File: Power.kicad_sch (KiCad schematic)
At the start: 70 parts, among them J11 Conn_01x02_Socket, Q3 2N2222, U19 TPS25983, U20 SiA462DJ, U21 MIC23201YML-TR, U29 AP7361C-33E, U30 MP8795

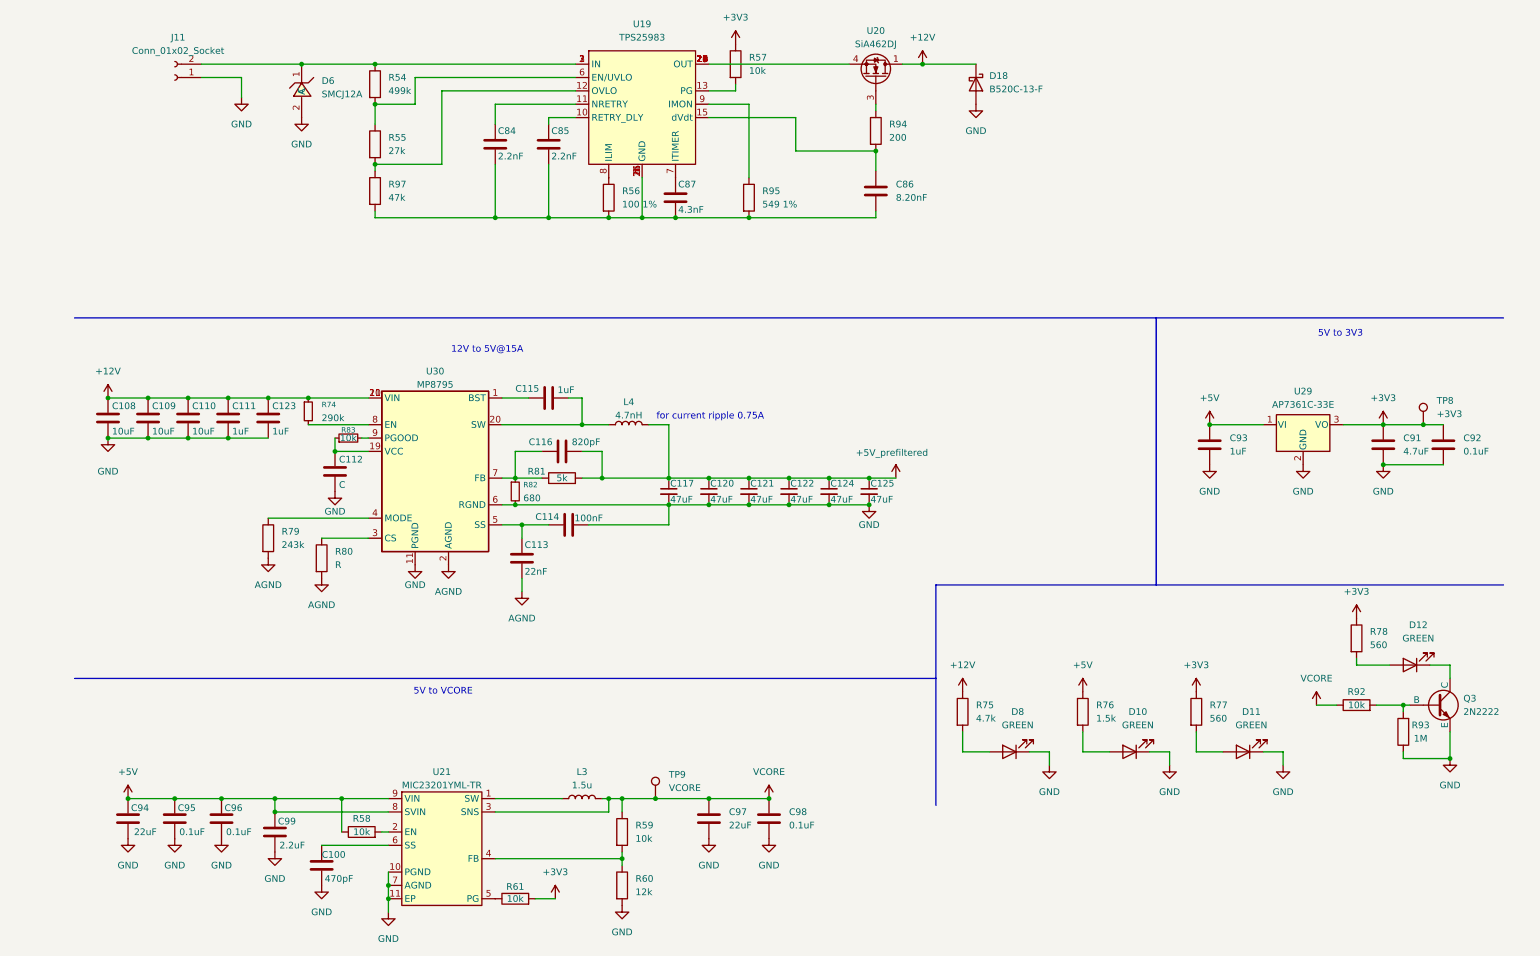
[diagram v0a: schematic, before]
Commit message: Ferrite bread filter for LDO and MIC23201, labelling improved
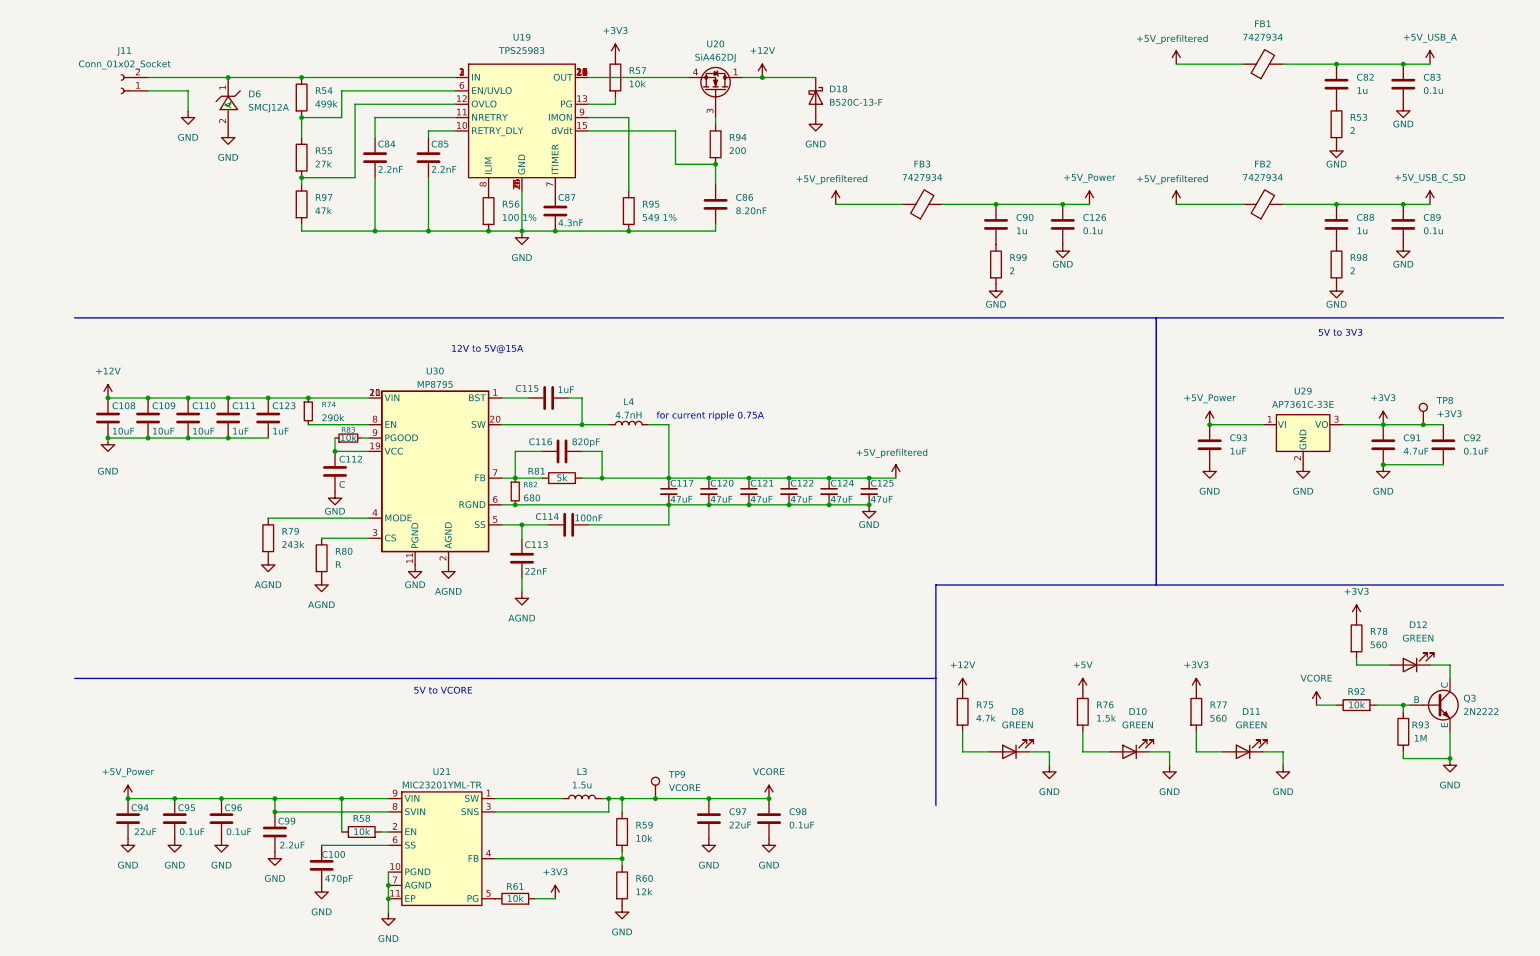
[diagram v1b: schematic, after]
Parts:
- added C126, C83, C89: 0.1u, symbol Device:C
- added C82, C88, C90: 1u, symbol Device:C
- added FB1, FB2, FB3: 7427934, symbol Device:FerriteBead
- added R53, R98, R99: 2, symbol Device:R
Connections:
- net +5V: no longer C93.1, C94.1, C95.1, C96.1, C99.1, R58.1, U21.8 (SVIN), U21.9 (VIN), U29.1 (VI)
- net +5V_prefiltered: now also FB1.1, FB2.1, FB3.1
- net GND: now also C84.2, C85.2, C86.2, C87.2, R56.2, R95.2, R97.2, U19.14 (GND), U19.26 (GND), U19.4 (GND), U19.5 (GND), C126.2, C83.2, C89.2, R53.2, R98.2, R99.2
- new net: C90.2, R99.1
- new net: C82.2, R53.1
- new net: C88.2, R98.1
- new net +5V_Power: C126.1, C90.1, C93.1, C94.1, C95.1, C96.1, C99.1, FB3.2, R58.1, U21.8 (SVIN), U21.9 (VIN), U29.1 (VI)
- new net +5V_USB_A: C82.1, C83.1, FB1.2
- new net +5V_USB_C_SD: C88.1, C89.1, FB2.2
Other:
- moved on the sheet: C84, C85, C86, C87, D18, D6, J11, R54, R55, R56, R57, R94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

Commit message: Schematic reannotated
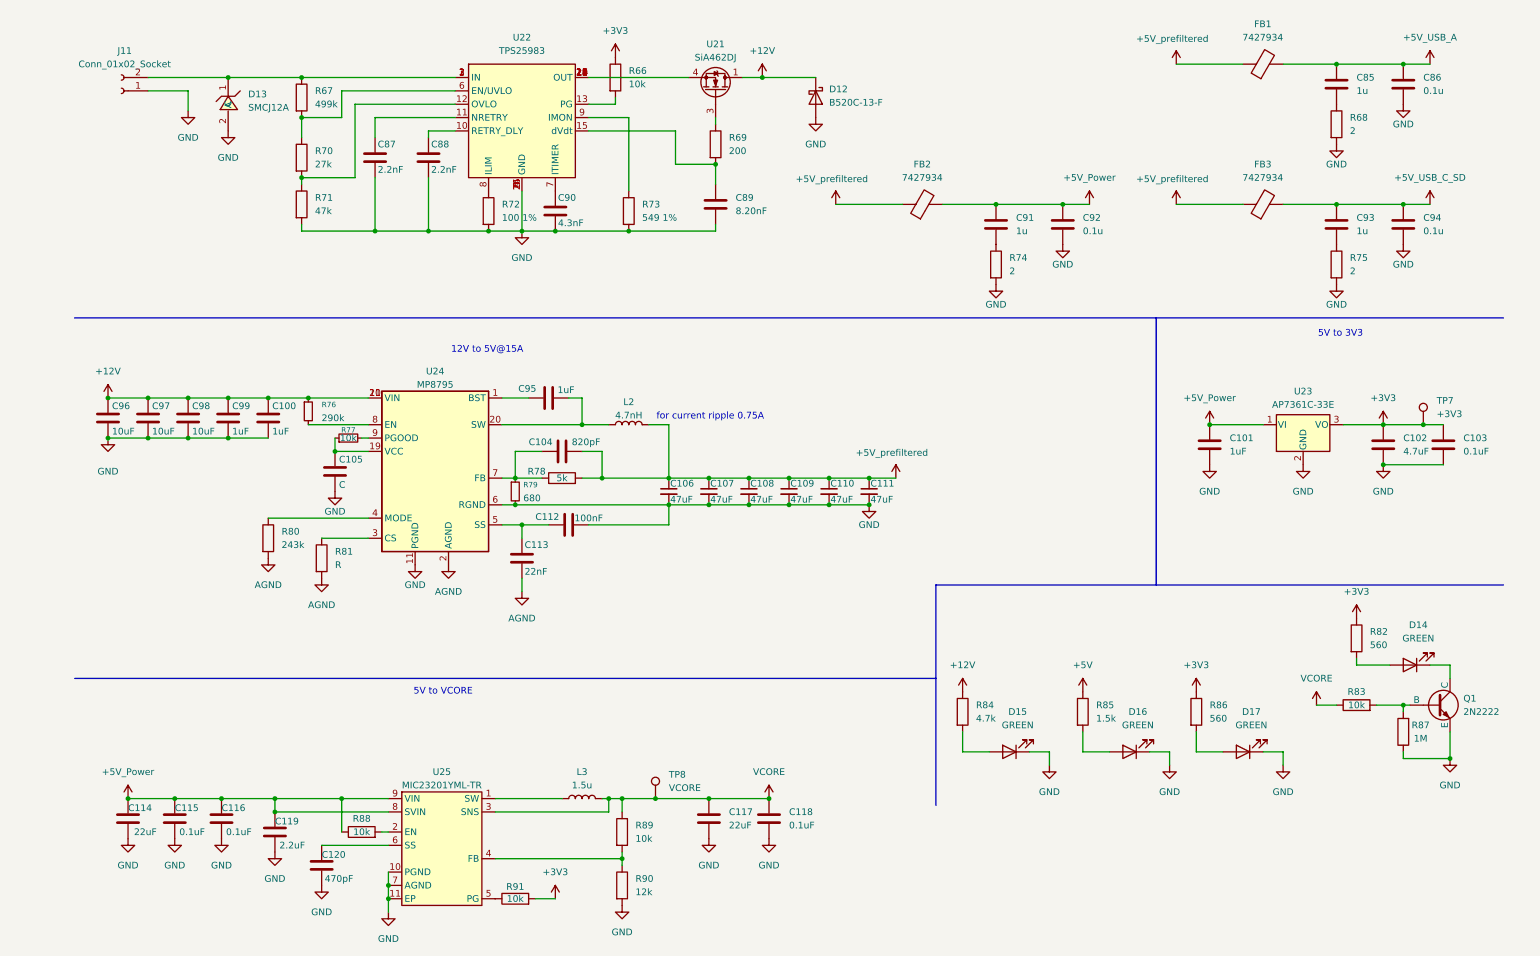
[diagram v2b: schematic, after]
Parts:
- renumbered C123 to C100, C93 to C101, C91 to C102, C92 to C103, C116 to C104, C112 to C105, C117 to C106, C120 to C107, C121 to C108, C122 to C109, C124 to C110, C125 to C111, C114 to C112, C94 to C114, C95 to C115, C96 to C116, C97 to C117, C98 to C118, C99 to C119, C100 to C120, C82 to C85, C83 to C86, C84 to C87, C85 to C88, C86 to C89, C87 to C90, C90 to C91, C126 to C92, C88 to C93, C89 to C94, C115 to C95, C108 to C96, C109 to C97, C110 to C98, C111 to C99, D18 to D12, D6 to D13, D12 to D14, D8 to D15, D10 to D16, D11 to D17, FB3 to FB2, FB2 to FB3, L4 to L2, Q3 to Q1, R57 to R66, R54 to R67, R53 to R68, R94 to R69, R55 to R70, R97 to R71, R56 to R72, R95 to R73, R99 to R74, R98 to R75, R74 to R76, R83 to R77, R81 to R78, R82 to R79, R79 to R80, R80 to R81, R78 to R82, R92 to R83, R75 to R84, R76 to R85, R77 to R86, R93 to R87, R58 to R88, R59 to R89, R60 to R90, R61 to R91, TP8 to TP7, TP9 to TP8, U20 to U21, U19 to U22, U29 to U23, U30 to U24, U21 to U25

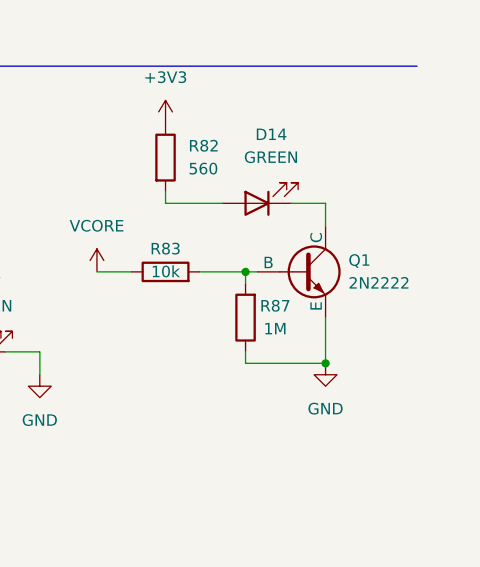
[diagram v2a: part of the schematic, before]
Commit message: Q1 changed to MMBT2222A
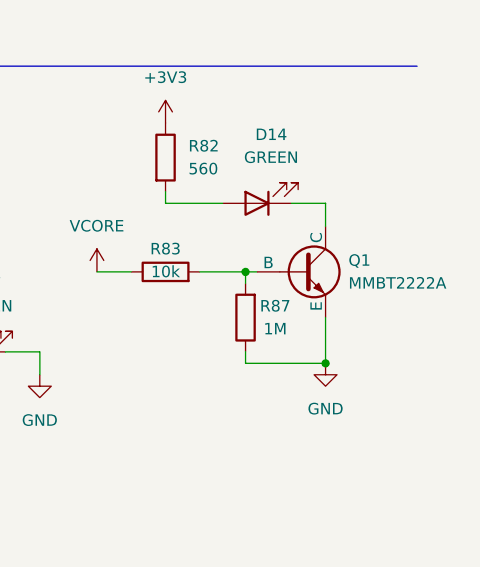
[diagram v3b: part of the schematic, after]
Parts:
- D12: footprint (none) -> Diode_SMD:D_SMC
- D13: footprint EasyEDA:X2SON-2_L0.6-W0.3-P0.35 -> Diode_SMD:D_SMC
- D14, D15, D16, D17: footprint (none) -> LED_SMD:LED_0603_1608Metric
- Q1: value 2N2222 -> MMBT2222A
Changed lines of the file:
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@@
 			)
 		)
-		(property "Footprint" ""
+		(property "Footprint" "LED_SMD:LED_0603_1608Metric"
 			(at 190.5 156.21 0)
 			(effects
@@
 			)
 		)
-		(property "Footprint" ""
+		(property "Footprint" "Diode_SMD:D_SMC"
 			(at 153.67 31.75 0)
 			(effects
@@
 			)
 		)
-		(property "Footprint" "EasyEDA:X2SON-2_L0.6-W0.3-P0.35"
+		(property "Footprint" "Diode_SMD:D_SMC"
 			(at 34.29 33.02 0)
 			(effects
@@
 			)
 		)
-		(property "Footprint" ""
+		(property "Footprint" "LED_SMD:LED_0603_1608Metric"
 			(at 234.95 156.21 0)
 			(effects
@@
 			)
 		)
-		(property "Footprint" ""
+		(property "Footprint" "LED_SMD:LED_0603_1608Metric"
 			(at 266.7 139.7 0)
 			(effects
@@
 			)
 		)
-		(property "Footprint" ""
+		(property "Footprint" "LED_SMD:LED_0603_1608Metric"
 			(at 213.36 156.21 0)
 			(effects
@@
 			)
 		)
-		(property "Value" "2N2222"
+		(property "Value" "MMBT2222A"
 			(at 276.86 148.5899 0)
 			(effects

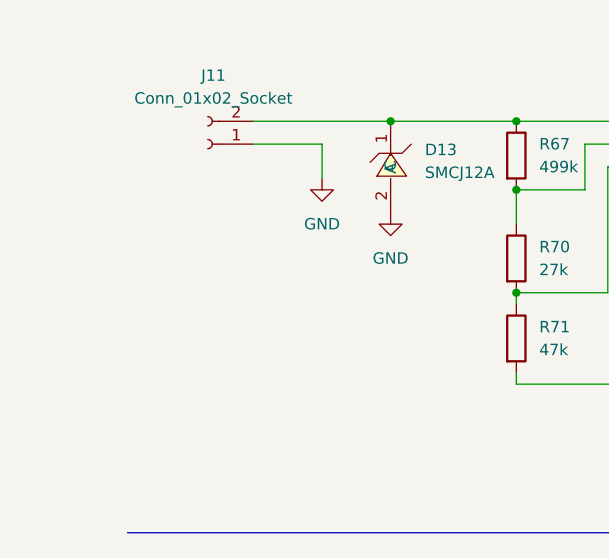
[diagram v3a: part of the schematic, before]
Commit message: J11 changed to 8-pin PCIe connector, footprint assigned
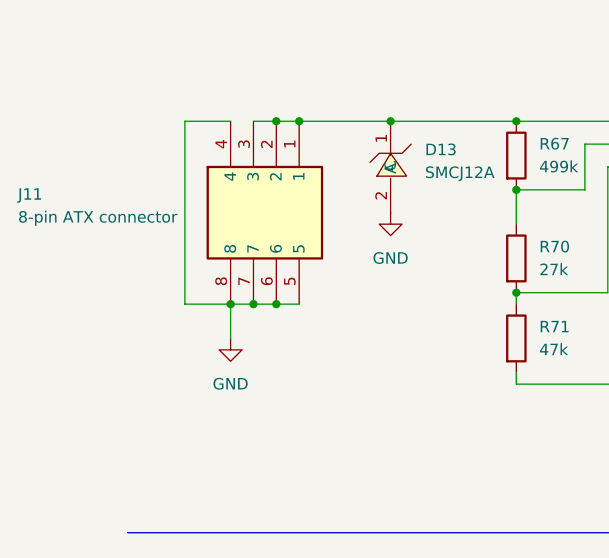
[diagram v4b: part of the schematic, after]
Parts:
- C100, C104, C105, C106, C107, C108, C109, C110, C111, C112, C113, C85, C86, C87, C88, C89, C90, C91, C92, C93, C94, C95, C96, C97, C98, C99: footprint (none) -> Capacitor_SMD:C_0402_1005Metric
- FB1, FB2, FB3: footprint (none) -> SamacSys_Parts:7427934
- J11: value Conn_01x02_Socket -> 8-pin ATX connector; footprint Connector_PinHeader_1.27mm:PinHeader_1x02_P1.27mm_Vertical -> SamacSys_Parts:45586-000Y; symbol Connector:Conn_01x02_Socket -> SamacSys_Parts:45586-0005; Height (none) -> 10; Manufacturer_Name (none) -> Molex; Manufacturer_Part_Number (none) -> 45586-0005; Mouser Part Number (none) -> 538-45586-0005; Mouser Price/Stock (none) -> https://www.mouser.co.uk/ProductDetail/Molex/45586-0005?qs=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
- L2: footprint (none) -> Inductor_SMD:L_6.3x6.3_H3
- Q1: footprint (none) -> Package_TO_SOT_SMD:SOT-23-3
- R66, R67, R68, R69, R70, R71, R72, R73, R74, R75, R76, R77, R78, R79, R80, R81, R82, R83, R84, R85, R86, R87: footprint (none) -> Resistor_SMD:R_0402_1005Metric
- U22: footprint (none) -> SamacSys_Parts:TPS259830ONRGER
- U24: footprint (none) -> Package_DFN_QFN:MPS-QFN-21_3x4mm
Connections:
- net GND: now also J11.4, J11.5, J11.6, J11.7, J11.8; no longer J11.1 (Pin_1)
- net at D13.1 (C), J11.2, R67.1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: now also J11.1, J11.3

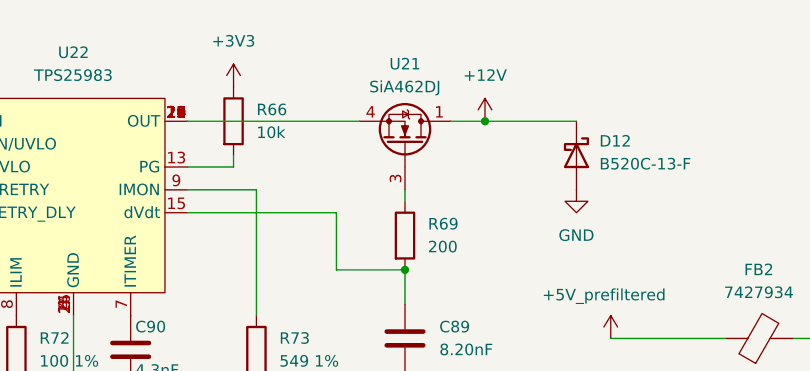
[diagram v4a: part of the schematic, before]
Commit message: footprints assigned, U21 change to SiRA80DP
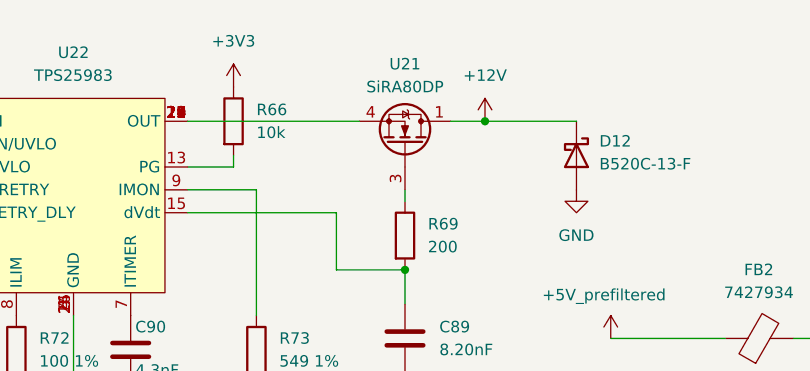
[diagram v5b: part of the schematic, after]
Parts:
- TP7, TP8: footprint TestPoint:TestPoint_THTPad_1.5x1.5mm_Drill0.7mm -> TestPoint:TestPoint_Loop_D1.80mm_Drill1.0mm_Beaded
- U21: value SiA462DJ -> SiRA80DP; footprint Package_TO_SOT_SMD:Vishay_PowerPAK_SC70-6L_Single -> Package_SO:PowerPAK_SO-8L_Single
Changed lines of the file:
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@@
 			)
 		)
-		(property "Footprint" "TestPoint:TestPoint_THTPad_1.5x1.5mm_Drill0.7mm"
+		(property "Footprint" "TestPoint:TestPoint_Loop_D1.80mm_Drill1.0mm_Beaded"
 			(at 128.27 165.1 0)
 			(effects
@@
 			)
 		)
-		(property "Footprint" "TestPoint:TestPoint_THTPad_1.5x1.5mm_Drill0.7mm"
+		(property "Footprint" "TestPoint:TestPoint_Loop_D1.80mm_Drill1.0mm_Beaded"
 			(at 274.32 93.98 0)
 			(effects
@@
 			)
 		)
-		(property "Value" "SiA462DJ"
+		(property "Value" "SiRA80DP"
 			(at 134.62 24.13 90)
 			(effects
@@
 			)
 		)
-		(property "Footprint" "Package_TO_SOT_SMD:Vishay_PowerPAK_SC70-6L_Single"
+		(property "Footprint" "Package_SO:PowerPAK_SO-8L_Single"
 			(at 129.54 25.4 0)
 			(effects
